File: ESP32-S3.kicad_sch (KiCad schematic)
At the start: 6 parts, among them U1 ESP32-S3-WROOM-1U-N16R8

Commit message: updated board design
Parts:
- U1: footprint ESP32_S3_WROOM_1U_N16R8:XCVR_ESP32-S3-WROOM-1U-N16R8 -> RF_Module:ESP32-S3-WROOM-1U
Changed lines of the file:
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@@
 			)
 		)
-		(property "Footprint" "ESP32_S3_WROOM_1U_N16R8:XCVR_ESP32-S3-WROOM-1U-N16R8"
+		(property "Footprint" "RF_Module:ESP32-S3-WROOM-1U"
 			(at 90.17 74.93 0)
 			(hide yes)

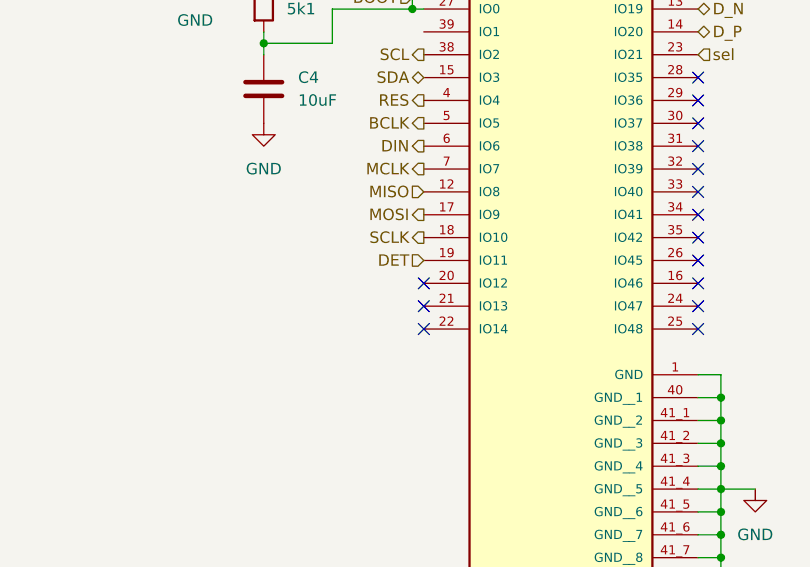
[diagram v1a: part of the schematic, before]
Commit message: updated board design to fit altoid tin
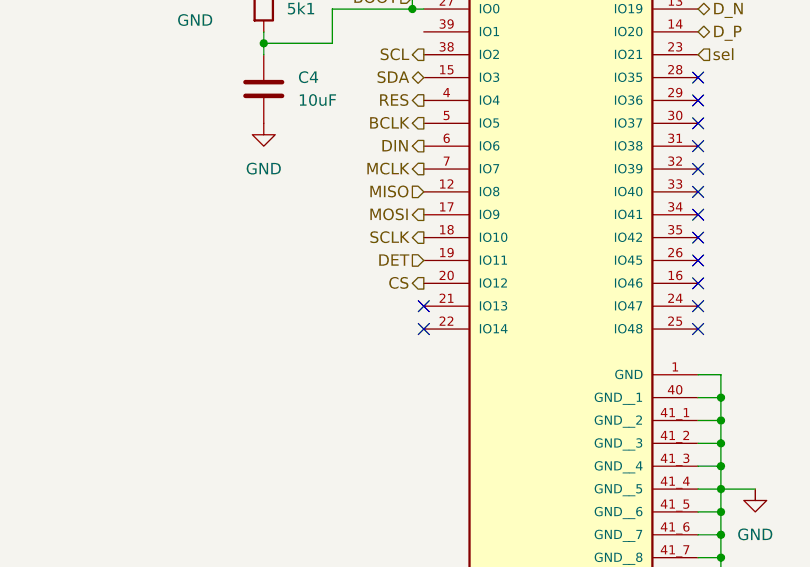
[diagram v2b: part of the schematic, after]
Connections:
- net CS: now reaches U1.20 (IO12)
- no-connect marks 17 -> 16
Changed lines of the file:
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@@
-	)
-	(no_connect
-		(at 74.93 92.71)
 	)
 	(no_connect
@@
 		(effects
 			(font
+				(size 1.27 1.27)
+			)
+			(justify right)
+		)
+	)
+	(hierarchical_label "CS"
+		(shape output)
+		(at 74.93 92.71 180)
+		(effects
+			(font
